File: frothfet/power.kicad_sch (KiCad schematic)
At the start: 51 parts, among them J1 Screw_Terminal_01x08, J2 Screw_Terminal_01x08, U27 TPS7A2033PDBVR, U28 MCP3425A0T-ECH, U29 REF35330QDBVR, U30 XL1509-5.0

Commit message: silkscreen done, erc+drc passing
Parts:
- R83: value 4.7k -> 100k
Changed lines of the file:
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@@
 	)
 	(junction
+		(at 96.52 101.6)
+		(diameter 0)
+		(color 0 0 0 0)
+	)
+	(junction
 		(at 41.91 170.18)
 		(diameter 0)
@@
 	)
 	(junction
-		(at 92.71 101.6)
-		(diameter 0)
-		(color 0 0 0 0)
-	)
-	(junction
 		(at 254 38.1)
 		(diameter 0)
@@
 	)
 	(junction
+		(at 92.71 101.6)
+		(diameter 0)
+		(color 0 0 0 0)
+	)
+	(junction
 		(at 59.69 128.27)
 		(diameter 0)
@@
 	)
 	(junction
+		(at 191.77 106.68)
+		(diameter 0)
+		(color 0 0 0 0)
+	)
+	(junction
 		(at 260.35 110.49)
 		(diameter 0)
@@
 	(wire
 		(pts
-			(xy 97.79 101.6) (xy 92.71 101.6)
-		)
-		(stroke
-			(width 0)
-			(type default)
-		)
-	)
-	(wire
-		(pts
 			(xy 128.27 125.73) (xy 148.59 125.73)
 		)
@@
 	(wire
 		(pts
+			(xy 39.37 110.49) (xy 39.37 114.3)
+		)
+		(stroke
+			(width 0)
+			(type default)
+		)
+	)
+	(wire
+		(pts
 			(xy 271.78 105.41) (xy 275.59 105.41)
 		)
@@
 	(wire
 		(pts
+			(xy 92.71 101.6) (xy 96.52 101.6)
+		)
+		(stroke
+			(width 0)
+			(type default)
+		)
+	)
+	(wire
+		(pts
 			(xy 254 45.72) (xy 254 44.45)
 		)
@@
 	(wire
 		(pts
-			(xy 194.31 106.68) (xy 189.23 106.68)
+			(xy 194.31 106.68) (xy 191.77 106.68)
 		)
 		(stroke
@@
 	(wire
 		(pts
+			(xy 90.17 101.6) (xy 92.71 101.6)
+		)
+		(stroke
+			(width 0)
+			(type default)
+		)
+	)
+	(wire
+		(pts
 			(xy 41.91 176.53) (xy 41.91 184.15)
 		)
@@
 	(wire
 		(pts
-			(xy 92.71 101.6) (xy 90.17 101.6)
-		)
-		(stroke
-			(width 0)
-			(type default)
-		)
-	)
-	(wire
-		(pts
 			(xy 68.58 38.1) (xy 68.58 43.18)
 		)
@@
 	(wire
 		(pts
+			(xy 191.77 106.68) (xy 189.23 106.68)
+		)
+		(stroke
+			(width 0)
+			(type default)
+		)
+	)
+	(wire
+		(pts
 			(xy 85.09 54.61) (xy 102.87 54.61)
 		)
@@
 	(wire
 		(pts
+			(xy 96.52 101.6) (xy 97.79 101.6)
+		)
+		(stroke
+			(width 0)
+			(type default)
+		)
+	)
+	(wire
+		(pts
 			(xy 271.78 107.95) (xy 275.59 107.95)
 		)
@@
 			)
 		)
-		(property "Value" "4.7k"
+		(property "Value" "100k"
 			(at 53.34 43.1799 0)
 			(effects
@@
 	)
 	(symbol
+		(lib_id "power:PWR_FLAG")
+		(at 191.77 106.68 0)
+		(unit 1)
+		(exclude_from_sim no)
+		(in_bom yes)
+		(on_board yes)
+		(dnp no)
+		(fields_autoplaced yes)
+		(property "Reference" "#FLG06"
+			(at 191.77 104.775 0)
+			(effects
+				(font
+					(size 1.27 1.27)
+				)
+				(hide yes)
+			)
+		)
+		(property "Value" "PWR_FLAG"
+			(at 191.77 101.6 0)
+			(effects
+				(font
+					(size 1.27 1.27)
+				)
+				(hide yes)
+			)
+		)
+		(property "Footprint" ""
+			(at 191.77 106.68 0)
+			(effects
+				(font
+					(size 1.27 1.27)
+				)
+				(hide yes)
+			)
+		)
+		(property "Datasheet" "~"
+			(at 191.77 106.68 0)
+			(effects
+				(font
+					(size 1.27 1.27)
+				)
+				(hide yes)
+			)
+		)
+		(property "Description" "Special symbol for telling ERC where power comes from"
+			(at 191.77 106.68 0)
+			(effects
+				(font
+					(size 1.27 1.27)
+				)
+				(hide yes)
+			)
+		)
+		(pin "1"
+		)
+		(instances
+			(project "frothfet"
+				(path "/c83c6236-96e9-46ad-9d7a-9e2efa4a7966/e112a34f-fd2f-43cb-bf5d-a7f5e57b6bef"
+					(reference "#FLG06")
+					(unit 1)
+				)
+			)
+		)
+	)
+	(symbol
 		(lib_id "Device:C_Small")
 		(at 151.13 45.72 0)
@@
 	)
 	(symbol
+		(lib_id "power:PWR_FLAG")
+		(at 39.37 110.49 0)
+		(unit 1)
+		(exclude_from_sim no)
+		(in_bom yes)
+		(on_board yes)
+		(dnp no)
+		(fields_autoplaced yes)
+		(property "Reference" "#FLG01"
+			(at 39.37 108.585 0)
+			(effects
+				(font
+					(size 1.27 1.27)
+				)
+				(hide yes)
+			)
+		)
+		(property "Value" "PWR_FLAG"
+			(at 39.37 105.41 0)
+			(effects
+				(font
+					(size 1.27 1.27)
+				)
+			)
+		)
+		(property "Footprint" ""
+			(at 39.37 110.49 0)
+			(effects
+				(font
+					(size 1.27 1.27)
+				)
+				(hide yes)
+			)
+		)
+		(property "Datasheet" "~"
+			(at 39.37 110.49 0)
+			(effects
+				(font
+					(size 1.27 1.27)
+				)
+				(hide yes)
+			)
+		)
+		(property "Description" "Special symbol for telling ERC where power comes from"
+			(at 39.37 110.49 0)
+			(effects
+				(font
+					(size 1.27 1.27)
+				)
+				(hide yes)
+			)
+		)
+		(pin "1"
+		)
+		(instances
+			(project ""
+				(path "/c83c6236-96e9-46ad-9d7a-9e2efa4a7966/e112a34f-fd2f-43cb-bf5d-a7f5e57b6bef"
+					(reference "#FLG01")
+					(unit 1)
+				)
+			)
+		)
+	)
+	(symbol
 		(lib_id "Connector:Screw_Terminal_01x08")
 		(at 251.46 110.49 0)
@@
 			)
 		)
+		(property "Sim.Pins" "1=K 2=A"
+			(at 50.8 49.53 0)
+			(effects
+				(font
+					(size 1.27 1.27)
+				)
+				(hide yes)
+			)
+		)
 		(pin "1"
 		)
@@
 			)
 		)
+		(property "Sim.Pins" "1=K 2=A"
+			(at 254 49.53 0)
+			(effects
+				(font
+					(size 1.27 1.27)
+				)
+				(hide yes)
+			)
+		)
 		(pin "1"
 		)
@@
 	(symbol
 		(lib_id "power:PWR_FLAG")
-		(at 176.53 69.85 0)
+		(at 96.52 101.6 0)
 		(unit 1)
 		(exclude_from_sim no)
@@
 		(dnp no)
 		(fields_autoplaced yes)
-		(property "Reference" "#FLG06"
-			(at 176.53 67.945 0)
+		(property "Reference" "#FLG012"
+			(at 96.52 99.695 0)
 			(effects
 				(font
@@
 		)
 		(property "Value" "PWR_FLAG"
-			(at 176.53 64.77 0)
+			(at 96.52 96.52 0)
 			(effects
 				(font
 					(size 1.27 1.27)
 				)
+				(hide yes)
 			)
 		)
 		(property "Footprint" ""
-			(at 176.53 69.85 0)
+			(at 96.52 101.6 0)
 			(effects
 				(font
@@
 		)
 		(property "Datasheet" "~"
-			(at 176.53 69.85 0)
+			(at 96.52 101.6 0)
 			(effects
 				(font
@@
 		)
 		(property "Description" "Special symbol for telling ERC where power comes from"
-			(at 176.53 69.85 0)
+			(at 96.52 101.6 0)
 			(effects
 				(font
@@
 		)
 		(instances
-			(project "8ch-mosfet"
+			(project ""
 				(path "/c83c6236-96e9-46ad-9d7a-9e2efa4a7966/e112a34f-fd2f-43cb-bf5d-a7f5e57b6bef"
-					(reference "#FLG06")
+					(reference "#FLG012")
 					(unit 1)
 				)

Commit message: bom and placement all check out.  ready for production!
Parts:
- C84: LCSC (none) -> C527225
- C89, R86: now not fitted
- D36, D43: value LED -> RED
- R89: value 1k -> 10k
- U29: Rotation Offset (none) -> 90
- U30: Rotation Offset (none) -> 180
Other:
- moved on the sheet: D39
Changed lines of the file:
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@@
 	(wire
 		(pts
-			(xy 92.71 128.27) (xy 92.71 127)
+			(xy 92.71 128.27) (xy 92.71 123.19)
 		)
 		(stroke
@@
 	(wire
 		(pts
-			(xy 92.71 114.3) (xy 92.71 119.38)
+			(xy 92.71 114.3) (xy 92.71 115.57)
 		)
 		(stroke
@@
 			)
 		)
-		(property "LCSC" ""
+		(property "LCSC" "C527225"
 			(at 82.55 123.19 0)
 			(effects
@@
 			)
 		)
-		(property "Value" "1k"
+		(property "Value" "10k"
 			(at 256.54 43.1799 0)
 			(effects
@@
 			)
 		)
-		(property "Value" "LED"
+		(property "Value" "RED"
 			(at 54.61 52.3874 90)
 			(effects
@@
 			)
 		)
+		(property "Rotation Offset" "90"
+			(at 148.59 115.57 0)
+			(effects
+				(font
+					(size 1.27 1.27)
+				)
+				(hide yes)
+			)
+		)
 		(pin "1"
 		)
@@
 			)
 		)
+		(property "Rotation Offset" "180"
+			(at 176.53 40.64 0)
+			(effects
+				(font
+					(size 1.27 1.27)
+				)
+				(hide yes)
+			)
+		)
 		(pin "1"
 		)
@@
 		(in_bom yes)
 		(on_board yes)
-		(dnp no)
+		(dnp yes)
 		(fields_autoplaced yes)
 		(property "Reference" "C89"
@@
 			)
 		)
-		(property "Value" "LED"
+		(property "Value" "RED"
 			(at 257.81 52.3874 90)
 			(effects
@@
 		(in_bom yes)
 		(on_board yes)
-		(dnp no)
+		(dnp yes)
 		(fields_autoplaced yes)
 		(property "Reference" "R86"
@@
 	(symbol
 		(lib_id "Device:D_TVS")
-		(at 92.71 123.19 90)
+		(at 92.71 119.38 90)
 		(unit 1)
 		(exclude_from_sim no)
@@
 		(dnp no)
 		(property "Reference" "D39"
-			(at 95.25 121.92 90)
+			(at 95.25 118.11 90)
 			(effects
 				(font
@@
 		)
 		(property "Value" "PESD3V3L1BA"
-			(at 95.25 124.46 90)
+			(at 95.25 120.65 90)
 			(effects
 				(font
@@
 		)
 		(property "Footprint" "Diode_SMD:D_SOD-323"
-			(at 92.71 123.19 0)
+			(at 92.71 119.38 0)
 			(effects
 				(font
@@
 		)
 		(property "Datasheet" "~"
-			(at 92.71 123.19 0)
+			(at 92.71 119.38 0)
 			(effects
 				(font
@@
 		)
 		(property "Description" ""
-			(at 92.71 123.19 0)
+			(at 92.71 119.38 0)
 			(effects
 				(font
@@
 		)
 		(property "LCSC" "C316020"
-			(at 92.71 123.19 90)
+			(at 92.71 119.38 90)
 			(effects
 				(font

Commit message: updated busbar design and added button silkscreen
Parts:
- J1: footprint yarrboard:Busbar Rev E -> yarrboard:Frothfet Busbar Positive Rev E
- J2: footprint yarrboard:Busbar Rev E -> yarrboard:Frothfet Busbar Negative Rev E
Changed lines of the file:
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@@
 			)
 		)
-		(property "Footprint" "yarrboard:Busbar Rev E"
+		(property "Footprint" "yarrboard:Frothfet Busbar Positive Rev E"
 			(at 251.46 110.49 0)
 			(effects
@@
 			)
 		)
-		(property "Footprint" "yarrboard:Busbar Rev E"
+		(property "Footprint" "yarrboard:Frothfet Busbar Negative Rev E"
 			(at 266.7 110.49 0)
 			(effects

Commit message: pulled in updated esp32-s3 schematic
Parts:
- renumbered R81 to R83, R82 to R84, R83 to R85, R84 to R86, R85 to R87, R86 to R88, R87 to R89, R88 to R90, R89 to R91

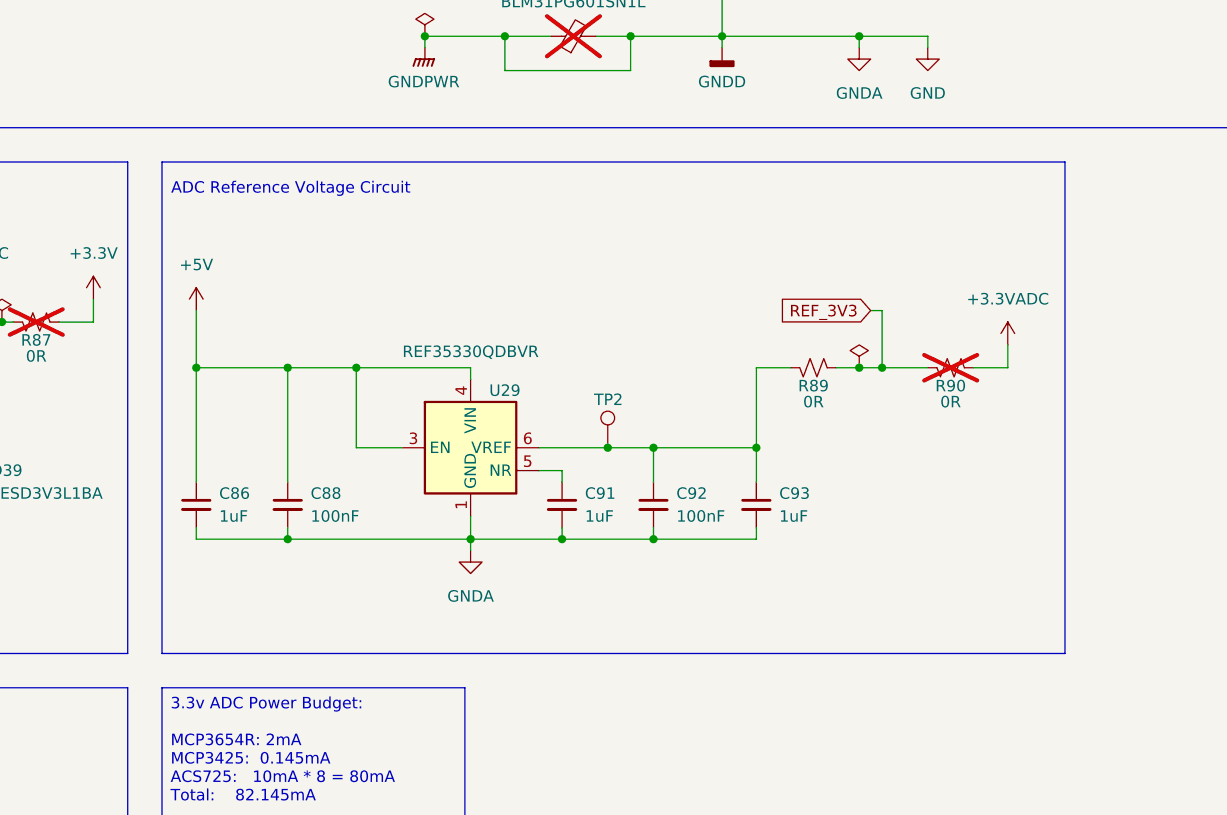
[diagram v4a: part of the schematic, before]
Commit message: removed adc and adc vref
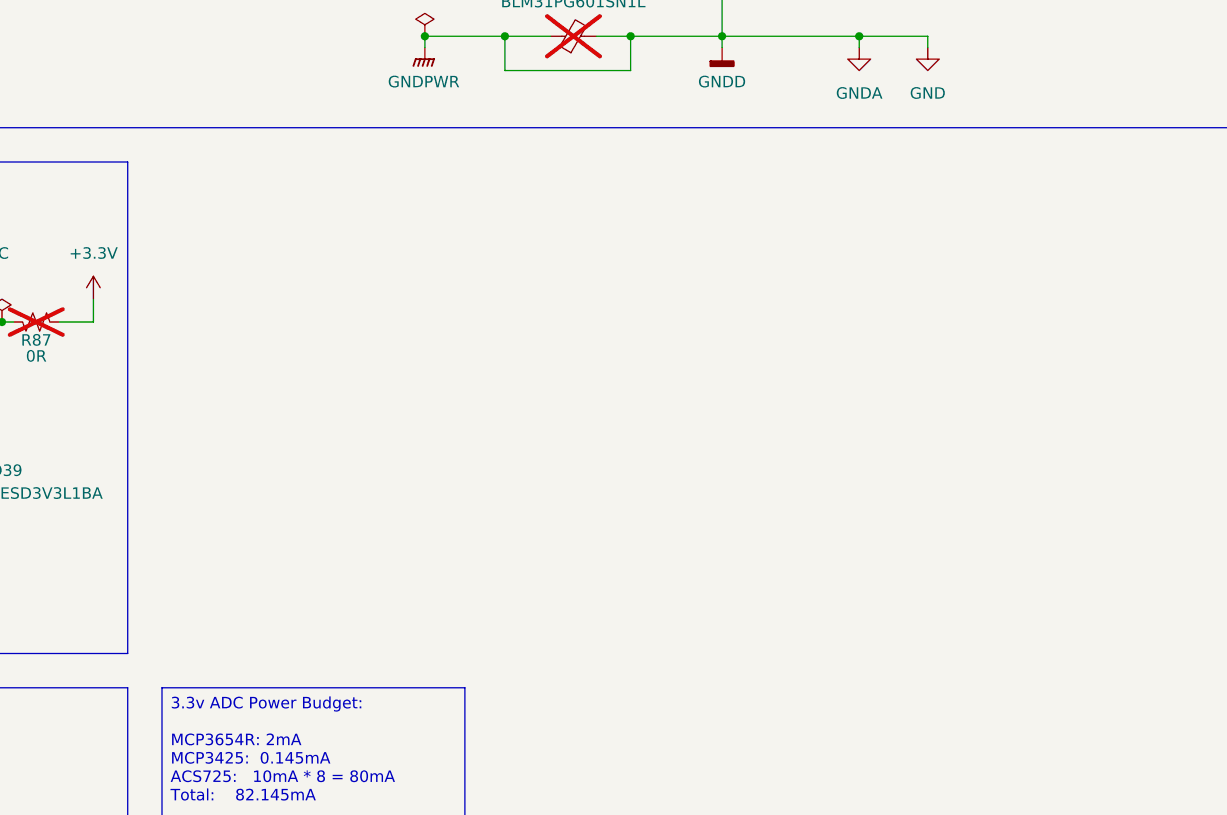
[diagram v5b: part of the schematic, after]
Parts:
- removed C86, C91, C93: 1uF, Capacitor_SMD:C_0603_1608Metric, symbol Device:C_Small
- removed C88, C92: 100nF, Capacitor_SMD:C_0603_1608Metric, symbol Device:C_Small
- removed R89, R90: 0R, Resistor_SMD:R_0603_1608Metric, symbol Device:R_Small_US
- removed TP2: TestPoint, TestPoint:TestPoint_THTPad_D2.0mm_Drill1.0mm, symbol Connector:TestPoint
- removed U29: REF35330QDBVR, Package_TO_SOT_SMD:SOT-23-6, symbol Reference_Voltage:REF35330QDBVR
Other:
- note removed: "ADC Reference Voltage Circuit"

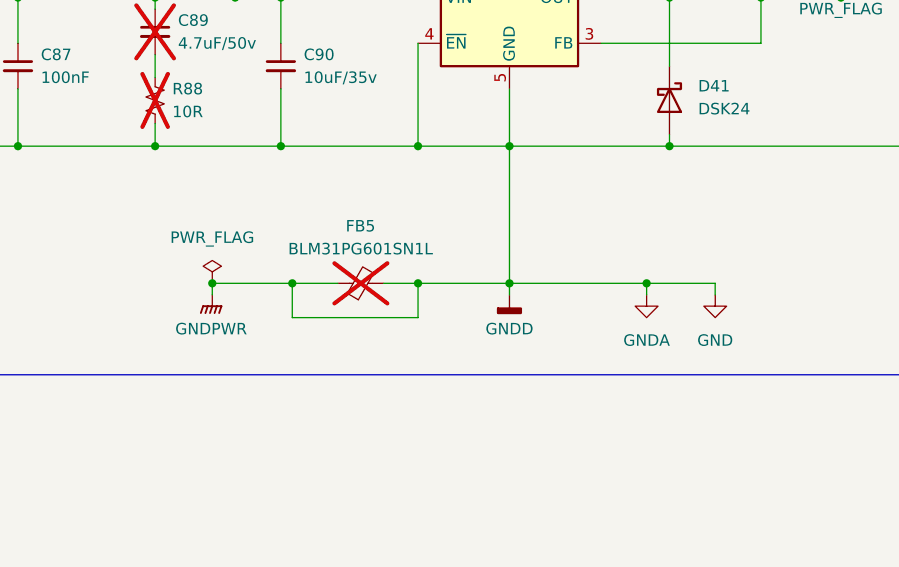
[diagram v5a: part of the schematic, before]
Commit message: removed unneccesary bleed circuit
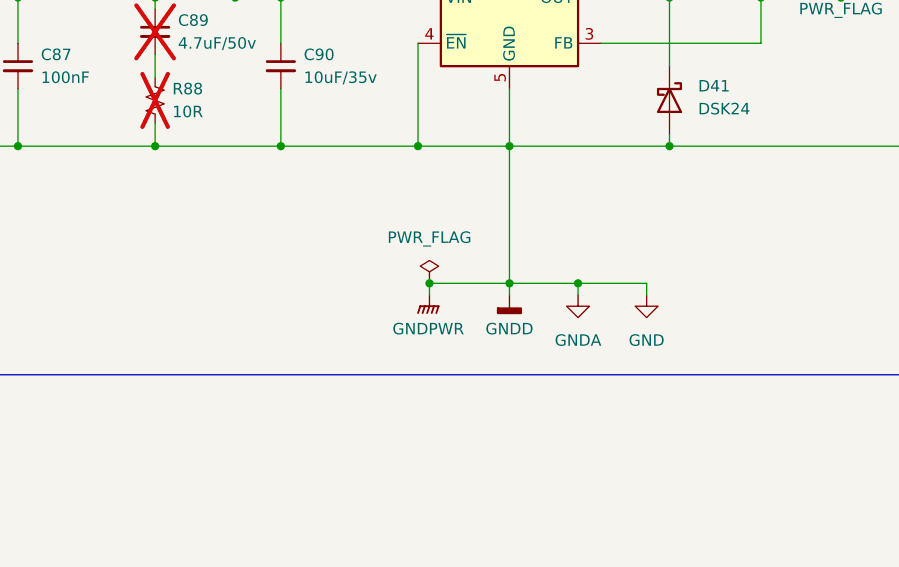
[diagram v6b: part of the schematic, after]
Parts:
- removed FB5: BLM31PG601SN1L, Inductor_SMD:L_1206_3216Metric, symbol Device:FerriteBead_Small
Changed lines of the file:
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@@
 	)
 	(junction
-		(at 191.77 69.85)
+		(at 184.15 69.85)
 		(diameter 0)
 		(color 0 0 0 0)
@@
 	)
 	(junction
-		(at 166.37 69.85)
-		(diameter 0)
-		(color 0 0 0 0)
-	)
-	(junction
 		(at 72.39 184.15)
 		(diameter 0)
@@
 	)
 	(junction
-		(at 143.51 69.85)
+		(at 167.64 69.85)
 		(diameter 0)
 		(color 0 0 0 0)
@@
 	)
 	(junction
-		(at 152.4 69.85)
-		(diameter 0)
-		(color 0 0 0 0)
-	)
-	(junction
 		(at 275.59 105.41)
 		(diameter 0)
@@
 	(wire
 		(pts
-			(xy 152.4 69.85) (xy 157.48 69.85)
-		)
-		(stroke
-			(width 0)
-			(type default)
-		)
-	)
-	(wire
-		(pts
 			(xy 49.53 124.46) (xy 49.53 128.27)
 		)
@@
 	(wire
 		(pts
-			(xy 152.4 73.66) (xy 152.4 69.85)
-		)
-		(stroke
-			(width 0)
-			(type default)
-		)
-	)
-	(wire
-		(pts
 			(xy 41.91 119.38) (xy 39.37 119.38)
 		)
@@
 	(wire
 		(pts
-			(xy 166.37 69.85) (xy 176.53 69.85)
-		)
-		(stroke
-			(width 0)
-			(type default)
-		)
-	)
-	(wire
-		(pts
 			(xy 204.47 38.1) (xy 204.47 43.18)
 		)
@@
 	(wire
 		(pts
-			(xy 191.77 69.85) (xy 199.39 69.85)
+			(xy 184.15 69.85) (xy 191.77 69.85)
 		)
 		(stroke
@@
 	(wire
 		(pts
-			(xy 162.56 69.85) (xy 166.37 69.85)
-		)
-		(stroke
-			(width 0)
-			(type default)
-		)
-	)
-	(wire
-		(pts
 			(xy 275.59 102.87) (xy 271.78 102.87)
 		)
@@
 	(wire
 		(pts
-			(xy 166.37 69.85) (xy 166.37 73.66)
-		)
-		(stroke
-			(width 0)
-			(type default)
-		)
-	)
-	(wire
-		(pts
 			(xy 204.47 43.18) (xy 186.69 43.18)
 		)
@@
 	(wire
 		(pts
-			(xy 191.77 71.12) (xy 191.77 69.85)
+			(xy 184.15 71.12) (xy 184.15 69.85)
 		)
 		(stroke
@@
 	(wire
 		(pts
-			(xy 166.37 73.66) (xy 152.4 73.66)
-		)
-		(stroke
-			(width 0)
-			(type default)
-		)
-	)
-	(wire
-		(pts
 			(xy 76.2 36.83) (xy 76.2 38.1)
 		)
@@
 	(wire
 		(pts
-			(xy 143.51 69.85) (xy 152.4 69.85)
+			(xy 167.64 69.85) (xy 176.53 69.85)
 		)
 		(stroke
@@
 	(wire
 		(pts
-			(xy 199.39 69.85) (xy 199.39 71.12)
+			(xy 191.77 69.85) (xy 191.77 71.12)
 		)
 		(stroke
@@
 	(wire
 		(pts
-			(xy 191.77 69.85) (xy 176.53 69.85)
+			(xy 184.15 69.85) (xy 176.53 69.85)
 		)
 		(stroke
@@
 	(wire
 		(pts
-			(xy 143.51 69.85) (xy 143.51 71.12)
+			(xy 167.64 69.85) (xy 167.64 71.12)
 		)
 		(stroke
@@
 	(symbol
 		(lib_id "power:PWR_FLAG")
-		(at 143.51 69.85 0)
+		(at 167.64 69.85 0)
 		(unit 1)
 		(exclude_from_sim no)
@@
 		(fields_autoplaced yes)
 		(property "Reference" "#FLG09"
-			(at 143.51 67.945 0)
+			(at 167.64 67.945 0)
 			(effects
 				(font
@@
 		)
 		(property "Value" "PWR_FLAG"
-			(at 143.51 64.77 0)
+			(at 167.64 64.77 0)
 			(effects
 				(font
@@
 		)
 		(property "Footprint" ""
-			(at 143.51 69.85 0)
+			(at 167.64 69.85 0)
 			(effects
 				(font
@@
 		)
 		(property "Datasheet" "~"
-			(at 143.51 69.85 0)
+			(at 167.64 69.85 0)
 			(effects
 				(font
@@
 		)
 		(property "Description" "Special symbol for telling ERC where power comes from"
-			(at 143.51 69.85 0)
+			(at 167.64 69.85 0)
 			(effects
 				(font
@@
 	(symbol
 		(lib_id "power:GNDPWR")
-		(at 143.51 71.12 0)
+		(at 167.64 71.12 0)
 		(unit 1)
 		(exclude_from_sim no)
@@
 		(fields_autoplaced yes)
 		(property "Reference" "#PWR0110"
-			(at 143.51 76.2 0)
+			(at 167.64 76.2 0)
 			(effects
 				(font
@@
 		)
 		(property "Value" "GNDPWR"
-			(at 143.383 74.93 0)
+			(at 167.513 74.93 0)
 			(effects
 				(font
@@
 		)
 		(property "Footprint" ""
-			(at 143.51 72.39 0)
+			(at 167.64 72.39 0)
 			(effects
 				(font
@@
 		)
 		(property "Datasheet" ""
-			(at 143.51 72.39 0)
+			(at 167.64 72.39 0)
 			(effects
 				(font
@@
 		)
 		(property "Description" "Power symbol creates a global label with name \"GNDPWR\" , global ground"
-			(at 143.51 71.12 0)
+			(at 167.64 71.12 0)
 			(effects
 				(font
@@
 	(symbol
 		(lib_id "power:GND")
-		(at 199.39 71.12 0)
+		(at 191.77 71.12 0)
 		(unit 1)
 		(exclude_from_sim no)
@@
 		(fields_autoplaced yes)
 		(property "Reference" "#PWR0114"
-			(at 199.39 77.47 0)
+			(at 191.77 77.47 0)
 			(effects
 				(font
@@
 		)
 		(property "Value" "GND"
-			(at 199.39 76.2 0)
+			(at 191.77 76.2 0)
 			(effects
 				(font
@@
 		)
 		(property "Footprint" ""
-			(at 199.39 71.12 0)
+			(at 191.77 71.12 0)
 			(effects
 				(font
@@
 		)
 		(property "Datasheet" ""
-			(at 199.39 71.12 0)
+			(at 191.77 71.12 0)
 			(effects
 				(font
@@
 		)
 		(property "Description" "Power symbol creates a global label with name \"GND\" , ground"
-			(at 199.39 71.12 0)
+			(at 191.77 71.12 0)
 			(effects
 				(font
@@
 	)
 	(symbol
-		(lib_id "Device:FerriteBead_Small")
-		(at 160.02 69.85 90)
-		(unit 1)
-		(exclude_from_sim no)
-		(in_bom yes)
-		(on_board yes)
-		(dnp yes)
-		(fields_autoplaced yes)
-		(property "Reference" "FB5"
-			(at 159.9819 63.5 90)
-			(effects
-				(font
-					(size 1.27 1.27)
-				)
-			)
-		)
-		(property "Value" "BLM31PG601SN1L"
-			(at 159.9819 66.04 90)
-			(effects
-				(font
-					(size 1.27 1.27)
-				)
-			)
-		)
-		(property "Footprint" "Inductor_SMD:L_1206_3216Metric"
-			(at 160.02 71.628 90)
-			(effects
-				(font
-					(size 1.27 1.27)
-				)
-				(hide yes)
-			)
-		)
-		(property "Datasheet" "~"
-			(at 160.02 69.85 0)
-			(effects
-				(font
-					(size 1.27 1.27)
-				)
-				(hide yes)
-			)
-		)
-		(property "Description" "Ferrite bead, small symbol"
-			(at 160.02 69.85 0)
-			(effects
-				(font
-					(size 1.27 1.27)
-				)
-				(hide yes)
-			)
-		)
-		(pin "1"
-		)
-		(pin "2"
-		)
-		(instances
-			(project "frothfet"
-				(path "/c83c6236-96e9-46ad-9d7a-9e2efa4a7966/e112a34f-fd2f-43cb-bf5d-a7f5e57b6bef"
-					(reference "FB5")
-					(unit 1)
-				)
-			)
-		)
-	)
-	(symbol
 		(lib_id "power:PWR_FLAG")
 		(at 96.52 101.6 0)
@@
 	(symbol
 		(lib_id "power:GNDA")
-		(at 191.77 71.12 0)
+		(at 184.15 71.12 0)
 		(unit 1)
 		(exclude_from_sim no)
@@
 		(fields_autoplaced yes)
 		(property "Reference" "#PWR0113"
-			(at 191.77 77.47 0)
+			(at 184.15 77.47 0)
 			(effects
 				(font
@@
 		)
 		(property "Value" "GNDA"
-			(at 191.77 76.2 0)
+			(at 184.15 76.2 0)
 			(effects
 				(font
@@
 		)
 		(property "Footprint" ""
-			(at 191.77 71.12 0)
+			(at 184.15 71.12 0)
 			(effects
 				(font
@@
 		)
 		(property "Datasheet" ""
-			(at 191.77 71.12 0)
+			(at 184.15 71.12 0)
 			(effects
 				(font
@@
 		)
 		(property "Description" "Power symbol creates a global label with name \"GNDA\" , analog ground"
-			(at 191.77 71.12 0)
+			(at 184.15 71.12 0)
 			(effects
 				(font
